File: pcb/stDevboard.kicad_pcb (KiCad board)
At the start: 4 copper layers, 50 x 100 mm, 149 parts, among them IC1 MPM3610GQV-Z, IC2 IRFR9014PBF, IC3 ICM-45686, IC4 ICM-45686, IC5 MMC5983MA, IC6 AT25SF041B-SSHB-B, J1 USB_C_Receptacle_USB2.0_16P, J10 Micro_SD_Card_Det2, J2 USB_C_Receptacle_USB2.0_16P, J4 Conn_02x03_Top_Bottom, J7 73412-0114, J8 73412-0114, Q1 DMN3404L, Q2 MMBT2222A, Q3 DMN3404L, Q4 DMN3404L, Q5 DMN3404L, Q6 DMN3404L, Q7 DMN3404L, Q8 MMBT2222A, U1 BMP581, U2 H3LIS331DLTR, U3 MAX-M10S, U4 STM32U585CIUxQ, U5 STM32U073CCUx, Y1 ECS-TXO-25CSMV-320-AM-TR, Y2 ECS-160-8-36B2-CKM-TR, Y3 CM7V-T1A-32.768KHZ, Y4 CM7V-T1A-32.768KHZ

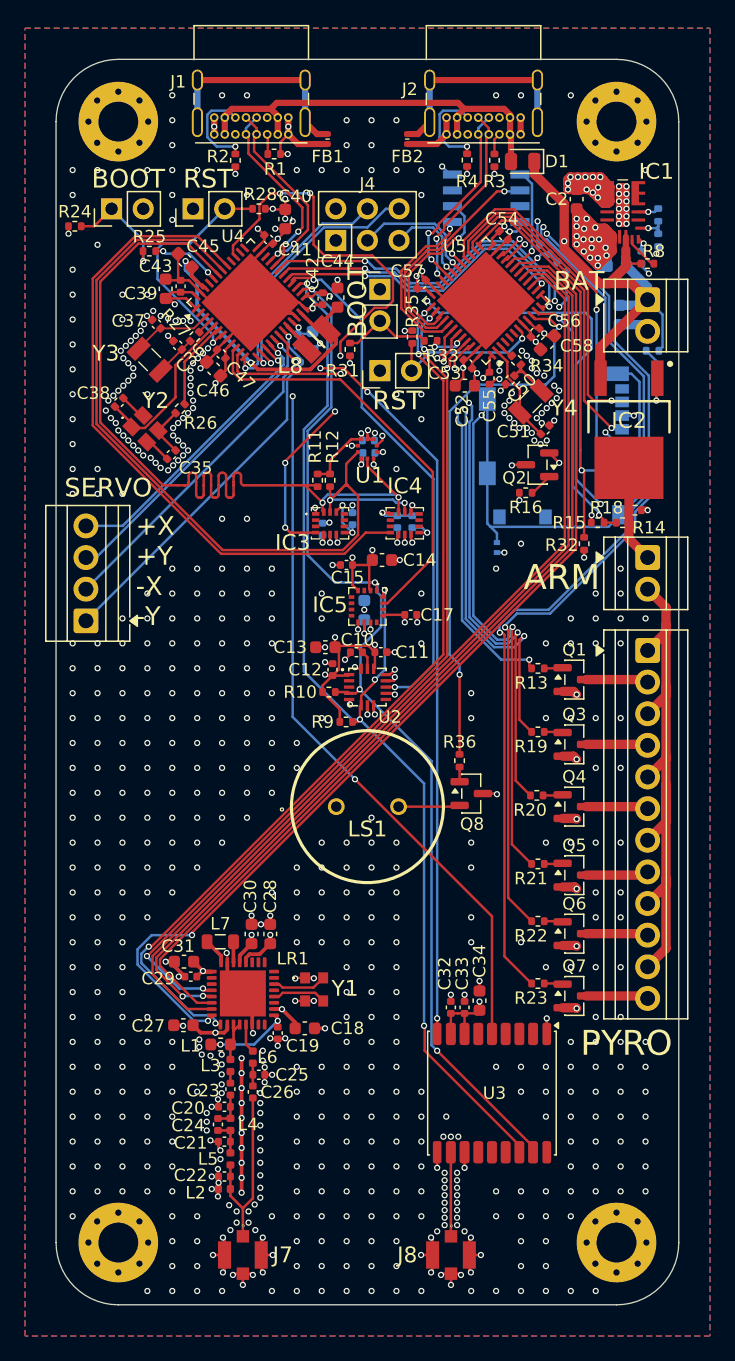
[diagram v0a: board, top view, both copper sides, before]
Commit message: updated pcb from schematic changes, also added some length tuning because why not
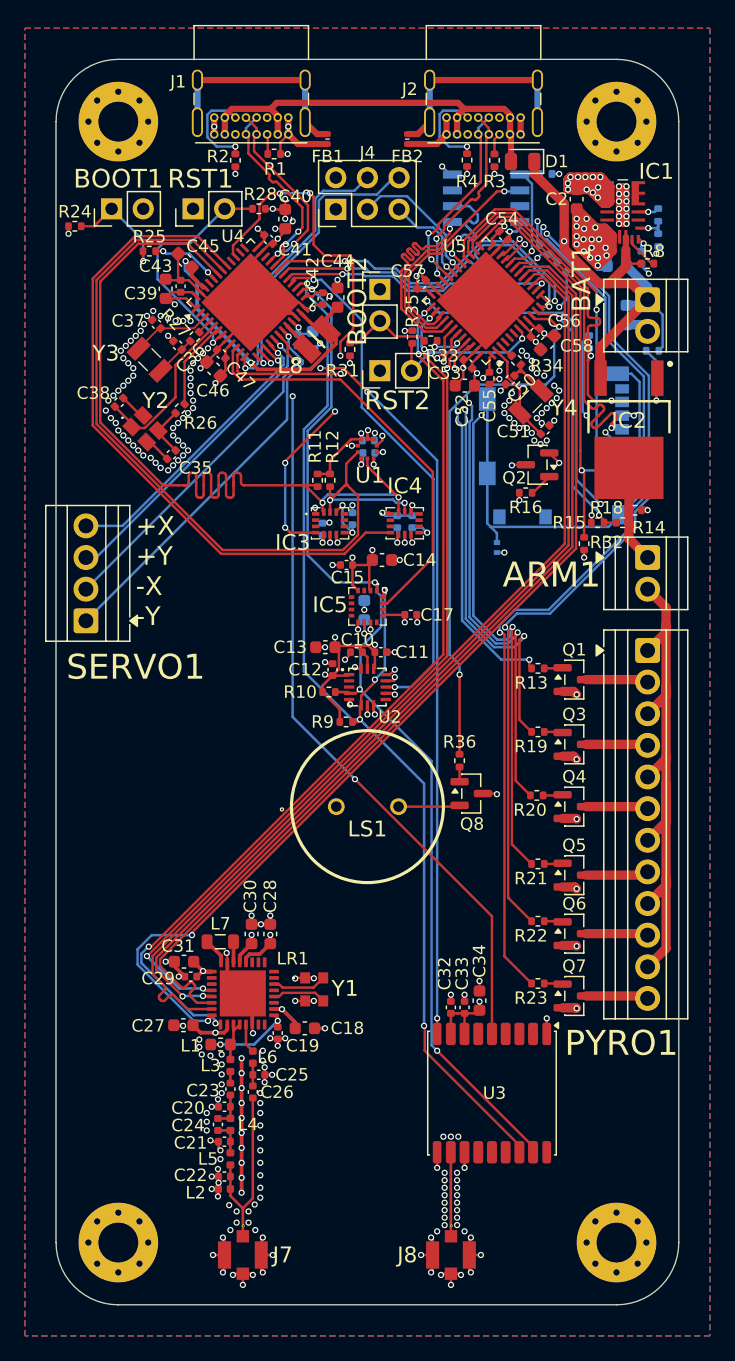
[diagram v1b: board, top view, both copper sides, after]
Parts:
- added R37: 10k, Resistor_SMD:R_0402_1005Metric, B.Cu at (139.3, 84.2)
- added R38: 100k, Resistor_SMD:R_0402_1005Metric, B.Cu at (142.8, 97.7)
- C1: value 100uF -> 22uF
- C39, C46: value 1 uF -> 1uF
- C4, C41, C42, C43, C47, C49, C5: value 100 nF -> 100nF
- C40, C48: value 10 uF -> 10uF
- C44, C45: value 2.2 uF -> 2.2uF
- moved J4 2.50 mm to (122.5, 87.0)
- moved C1 0.55 mm to (145.8, 95.5)
- turned R32 to 90 degrees
- renumbered ARM to ARM1, BAT to BAT1, BOOT to BOOT1, BOOT to BOOT2, PYRO to PYRO1, RST to RST1, RST to RST2, SERVO to SERVO1
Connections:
- R32 pad 1: /peripheral micro/sd_cs -> +3.3V
- R32 pad 2: +3.3V -> /peripheral micro/sd_cs
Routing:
- net +3.3V: track 129.9 -> 137.2 mm, vias 54 -> 56
- net /peripheral micro/sd_clk: track 25.9 -> 30.5 mm
- net usart_ck: track 24.4 -> 28.8 mm
- net /peripheral micro/flash_mosi: track 14.0 -> 18.4 mm
- net imu1_int1: track 48.2 -> 43.9 mm
- net /peripheral micro/flash_clk: track 14.7 -> 18.4 mm
- net /peripheral micro/sd_miso: track 25.7 -> 29.1 mm, vias 1 -> 2
- net mpu_tx_external: track 19.6 -> 22.1 mm
- net mpu_rx_external: track 20.4 -> 23.0 mm
- net arm: track 43.6 -> 41.6 mm
- net spi_sclk: track 77.5 -> 79.0 mm
- net usart_mosi: track 27.4 -> 28.9 mm
- net /peripheral micro/flash_cs: track 9.12 -> 10.5 mm
- net spi_mosi: track 77.9 -> 79.3 mm
- net GND: track 232.0 -> 231.1 mm, vias 713 -> 292
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
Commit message: mainly worked on bom (still just on google sheets), but while doing so fixed some issues and redid some component selection
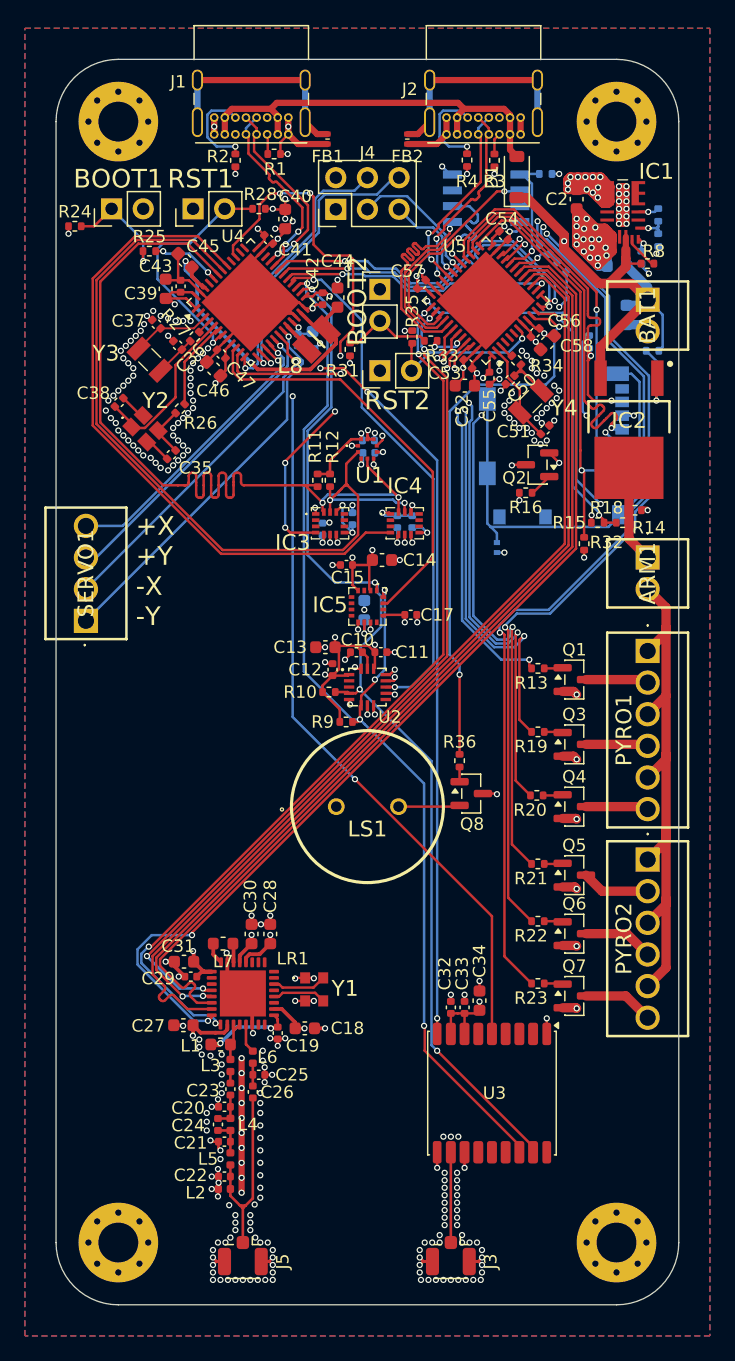
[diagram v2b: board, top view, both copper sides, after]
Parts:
- removed J7, J8: 73412-0114, footprints:73412-0110
- added J3: Conn_Coaxial, Connector_Coaxial:U.FL_Hirose_U.FL-R-SMT-1_Vertical, F.Cu at (131.7, 171.1)
- added J5: Conn_Coaxial, Connector_Coaxial:U.FL_Hirose_U.FL-R-SMT-1_Vertical, F.Cu at (115.0, 171.1)
- added PYRO2: Screw_Terminal_01x06, footprints:TBC05061GG, F.Cu at (147.5, 139.2)
- ARM1, BAT1: footprint TerminalBlock:TerminalBlock_Xinya_XY308-2.54-2P_1x02_P2.54mm_Horizontal -> footprints:TBC05021GG
- D1: footprint Diode_SMD:D_0805_2012Metric -> Diode_SMD:D_SOD-123
- L7: footprint Inductor_SMD:L_0805_2012Metric -> Inductor_SMD:L_0603_1608Metric
- PYRO1: value Screw_Terminal_01x12 -> Screw_Terminal_01x06; footprint TerminalBlock:TerminalBlock_Xinya_XY308-2.54-12P_1x12_P2.54mm_Horizontal -> footprints:TBC05061GG
- SERVO1: footprint TerminalBlock:TerminalBlock_Xinya_XY308-2.54-4P_1x04_P2.54mm_Horizontal -> footprints:TBC05041GG
- moved D1 1.33 mm to (137.0, 84.5), turned to 90 degrees
- moved L7 0.27 mm to (113.4, 146.0)
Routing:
- net GND: track 231.1 -> 219.5 mm, vias 292 -> 320
- net +3.3V: track 137.2 -> 139.7 mm
- net +BATT: track 49.3 -> 48.0 mm
- net +12C: track 46.9 -> 45.8 mm
- net Net-(J5-In): track 15.3 -> 16.3 mm
- net /mosfets/c5_n: track 5.00 -> 5.64 mm
- net /mosfets/c6_n: track 5.03 -> 5.67 mm
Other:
- board text added: "+0 -0 +1 -1 +2 -2 +3 -3 +4 -4 +5 -5"
- board text removed: "+1 -1 +2 -2 +3 -3 +4 -4 +5 -5 +6 -6"

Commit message: reorganized schematic, started to add a readme (not really though), also pcb updated
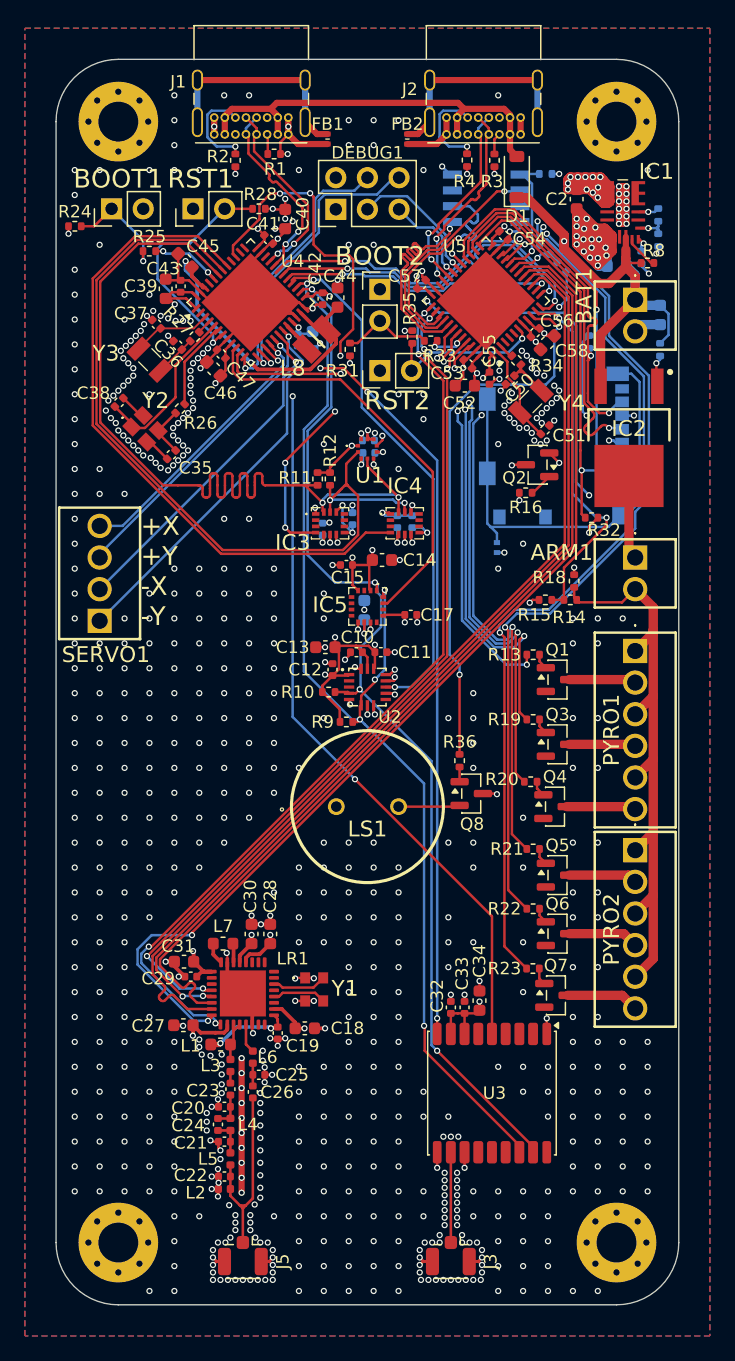
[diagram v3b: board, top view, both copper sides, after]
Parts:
- moved R18 7.50 mm to (141.6, 116.9), turned to -90 degrees
- moved R14 7.49 mm to (141.3, 118.4)
- moved R15 7.49 mm to (139.3, 118.4)
- moved C1 2.70 mm to (148.5, 95.5)
- moved R32 2.17 mm to (143.0, 111.8), turned to 180 degrees
- moved Q4 1.55 mm to (140.1, 135.0)
- moved Q7 1.48 mm to (140.1, 150.2)
- moved Q1 1.35 mm to (140.3, 124.8)
- moved Q3 1.35 mm to (140.3, 130.0)
- moved Q5 1.35 mm to (140.3, 140.5)
- moved Q6 1.35 mm to (140.3, 145.2)
- moved R23 1.26 mm to (138.3, 148.0)
- moved R21 1.26 mm to (138.3, 138.4)
- moved PYRO2 1.25 mm to (146.5, 138.5)
- moved R20 1.20 mm to (138.1, 133.0)
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- renumbered J4 to DEBUG1
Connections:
- net /shutupdrc renamed /x
- net Net-(IC5-CAP) renamed /sensors/mag_cap
- net Net-(J5-In) renamed /rf/lr_pre_rfin
- net Net-(LR1-RFI_LF) renamed /rf/lr_rfin
- net Net-(LR1-RFO_LF1) renamed /rf/lr_rfout
- net Net-(LR1-VTCXO/VNTC) renamed /rf/txco_vdd
- net Net-(LR1-XTA) renamed /rf/txco_out
- net Net-(RST1-Pin_2) renamed /main micro/reset
- net Net-(RST2-Pin_2) renamed /peripheral micro/reset
- net Net-(U4-PC14) renamed /main micro/lse_A
- net Net-(U4-PC15) renamed /main micro/lse_B
- net Net-(U4-PH0) renamed /main micro/hse_A
- net Net-(U4-PH1) renamed /main micro/hse_B
- net Net-(U4-PH3) renamed /main micro/boot
- net Net-(U5-PA0) renamed /peripheral micro/piezo
- net Net-(U5-PC13) renamed /peripheral micro/lse_A
- net Net-(U5-PC14) renamed /peripheral micro/lse_B
- net Net-(U5-PF3) renamed /peripheral micro/boot
- net imu3_int1 renamed accel_int1
- ARM1 pad 2: +12C -> +BATT_SWITCHED
- C10 pad 1: +3.3V -> GND
- C10 pad 2: GND -> +3.3V
- C11 pad 1: +3.3V -> GND
- C11 pad 2: GND -> +3.3V
- C12 pad 1: +3.3V -> GND
- C12 pad 2: GND -> +3.3V
- C13 pad 1: +3.3V -> GND
- C13 pad 2: GND -> +3.3V
- C28 pad 1: +3.3V -> GND
- C28 pad 2: GND -> +3.3V
- C30 pad 1: +3.3V -> GND
- C30 pad 2: GND -> +3.3V
- C32 pad 1: +3.3V -> GND
- C32 pad 2: GND -> +3.3V
- C35 pad 2: Net-(Y2-GND_1) -> GND
- C36 pad 1: GND -> Net-(C36-Pad1)
- C36 pad 2: Net-(C36-Pad2) -> GND
- C38 pad 2: Net-(Y2-GND_2) -> GND
- C39 pad 1: GND -> +3.3V
- C39 pad 2: +3.3V -> GND
- C40 pad 1: GND -> +3.3V
- C40 pad 2: +3.3V -> GND
- C41 pad 1: GND -> +3.3V
- C41 pad 2: +3.3V -> GND
- C42 pad 1: GND -> +3.3V
- C42 pad 2: +3.3V -> GND
- C43 pad 1: GND -> +3.3V
- C43 pad 2: +3.3V -> GND
- C44 pad 1: Net-(C44-Pad1) -> /main micro/vdd11
- C45 pad 1: Net-(C44-Pad1) -> /main micro/vdd11
- C46 pad 1: GND -> +3.3V
- C46 pad 2: +3.3V -> GND
- C47 pad 1: GND -> +3.3V
- C47 pad 2: +3.3V -> GND
- C50 pad 1: GND -> Net-(C50-Pad1)
- C50 pad 2: Net-(C50-Pad2) -> GND
- C52 pad 1: GND -> +3.3V
- C52 pad 2: +3.3V -> GND
- C53 pad 1: GND -> +3.3V
- C53 pad 2: +3.3V -> GND
- C54 pad 1: +3.3V -> GND
- C54 pad 2: GND -> +3.3V
- C55 pad 1: +3.3V -> GND
- C55 pad 2: GND -> +3.3V
- C56 pad 1: +3.3V -> GND
- C56 pad 2: GND -> +3.3V
- C57 pad 1: GND -> +3.3V
- C57 pad 2: +3.3V -> GND
- C58 pad 1: GND -> +3.3V
- C58 pad 2: +3.3V -> GND
- L8 pad 1: Net-(U4-VLXSMPS) -> /main micro/vdd11
- L8 pad 2: Net-(C44-Pad1) -> Net-(U4-VLXSMPS)
- PYRO1 pad 1: +12C -> +BATT_SWITCHED
- PYRO1 pad 2: /mosfets/c1_n -> /mosfets/c0_n
- PYRO1 pad 3: +12C -> +BATT_SWITCHED
- PYRO1 pad 4: /mosfets/c2_n -> /mosfets/c1_n
- PYRO1 pad 5: +12C -> +BATT_SWITCHED
- PYRO1 pad 6: /mosfets/c3_n -> /mosfets/c2_n
- PYRO2 pad 1: +12C -> +BATT_SWITCHED
- PYRO2 pad 2: /mosfets/c4_n -> /mosfets/c3_n
- PYRO2 pad 3: +12C -> +BATT_SWITCHED
- PYRO2 pad 4: /mosfets/c5_n -> /mosfets/c4_n
- PYRO2 pad 5: +12C -> +BATT_SWITCHED
- PYRO2 pad 6: /mosfets/c6_n -> /mosfets/c5_n
- Q1 pad 3: /mosfets/c1_n -> /mosfets/c0_n
- Q3 pad 3: /mosfets/c2_n -> /mosfets/c1_n
- Q4 pad 3: /mosfets/c3_n -> /mosfets/c2_n
- Q5 pad 3: /mosfets/c4_n -> /mosfets/c3_n
- Q6 pad 3: /mosfets/c5_n -> /mosfets/c4_n
- Q7 pad 3: /mosfets/c6_n -> /mosfets/c5_n
- R14 pad 2: Net-(ARM1-Pin_1) -> +BATT_SWITCHED
- R18 pad 1: Net-(ARM1-Pin_1) -> +3.3V
- R18 pad 2: +3.3V -> +BATT_SWITCHED
- R27 pad 1: Net-(C36-Pad2) -> Net-(C36-Pad1)
- R34 pad 1: Net-(C50-Pad2) -> Net-(C50-Pad1)
- U4 pad 23: Net-(C44-Pad1) -> /main micro/vdd11
- U4 pad 46: Net-(C44-Pad1) -> /main micro/vdd11
- U5 pad 12: usart_mosi -> usart_miso
- U5 pad 13: usart_miso -> usart_mosi
- Y2 pad 2: Net-(Y2-GND_1) -> GND
- Y2 pad 4: Net-(Y2-GND_2) -> GND
- Y3 pad 2: Net-(C36-Pad2) -> Net-(C36-Pad1)
- Y4 pad 2: Net-(C50-Pad2) -> Net-(C50-Pad1)
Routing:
- net +BATT_SWITCHED: track 0.00 -> 49.1 mm
- net +12C: track 45.8 -> 0.00 mm
- net Net-(C44-Pad1): track 27.3 -> 0.00 mm, vias 2 -> 0
- net /main micro/vdd11: track 0.00 -> 27.3 mm, vias 0 -> 2
- net cont_test_out: track 21.0 -> 29.1 mm
- net /mosfets/c6_n: track 5.67 -> 0.00 mm
- net /mosfets/c0_n: track 0.00 -> 5.40 mm
- net Net-(C50-Pad2): track 4.27 -> 0.00 mm
- net Net-(C50-Pad1): track 0.00 -> 4.27 mm
- net Net-(C36-Pad2): track 3.36 -> 0.00 mm
- net Net-(C36-Pad1): track 0.00 -> 3.36 mm
- net +BATT: track 48.0 -> 45.6 mm
- net Net-(Y2-GND_1): track 2.20 -> 0.00 mm
- net Net-(Y2-GND_2): track 2.18 -> 0.00 mm
- net GND: track 219.5 -> 217.3 mm, vias 320 -> 718
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
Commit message: added camera high side switching
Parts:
- added CAM1: Screw_Terminal_01x02, footprints:TBC05021GG, F.Cu at (103.5, 137.5)
- added IC7: IRFR9014PBF, footprints:TO228P990X238-3N, F.Cu at (111.5, 131.9)
- added Q9: MMBT2222A, Package_TO_SOT_SMD:SOT-23, F.Cu at (115.1, 124.0)
- added R39: 1k, Resistor_SMD:R_0402_1005Metric, F.Cu at (114.2, 121.1)
- added R40: 10k, Resistor_SMD:R_0402_1005Metric, F.Cu at (111.5, 125.5)
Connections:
- U5 pad 34: unconnected-(U5-PA13-Pad34) -> cam_enable
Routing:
- net +BATT: track 45.6 -> 114.4 mm, vias 2 -> 5
- net cam_enable: track 0.00 -> 39.7 mm, vias 0 -> 5
- net Net-(CAM1-Pin_2): track 0.00 -> 8.00 mm
- net GND: track 217.3 -> 224.9 mm, vias 718 -> 682
- net Net-(IC7-G): track 0.00 -> 6.03 mm
- net +3.3V: track 138.7 -> 142.9 mm, vias 56 -> 55
- net Net-(IC2-G): track 18.0 -> 15.2 mm
- net Net-(Q9-B): track 0.00 -> 1.46 mm
- net arm: track 39.8 -> 39.1 mm
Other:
- board text added: "+ -"

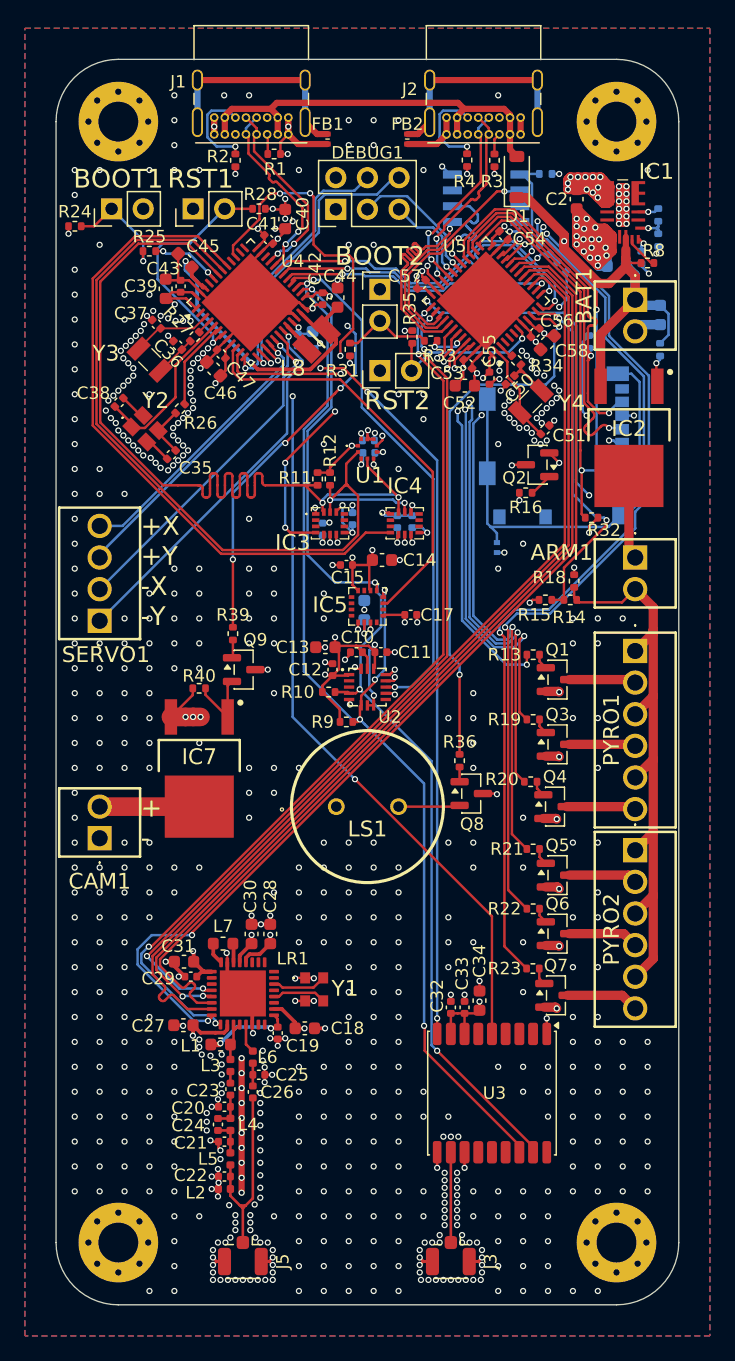
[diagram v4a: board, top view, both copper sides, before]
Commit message: modified gps for an active antenna
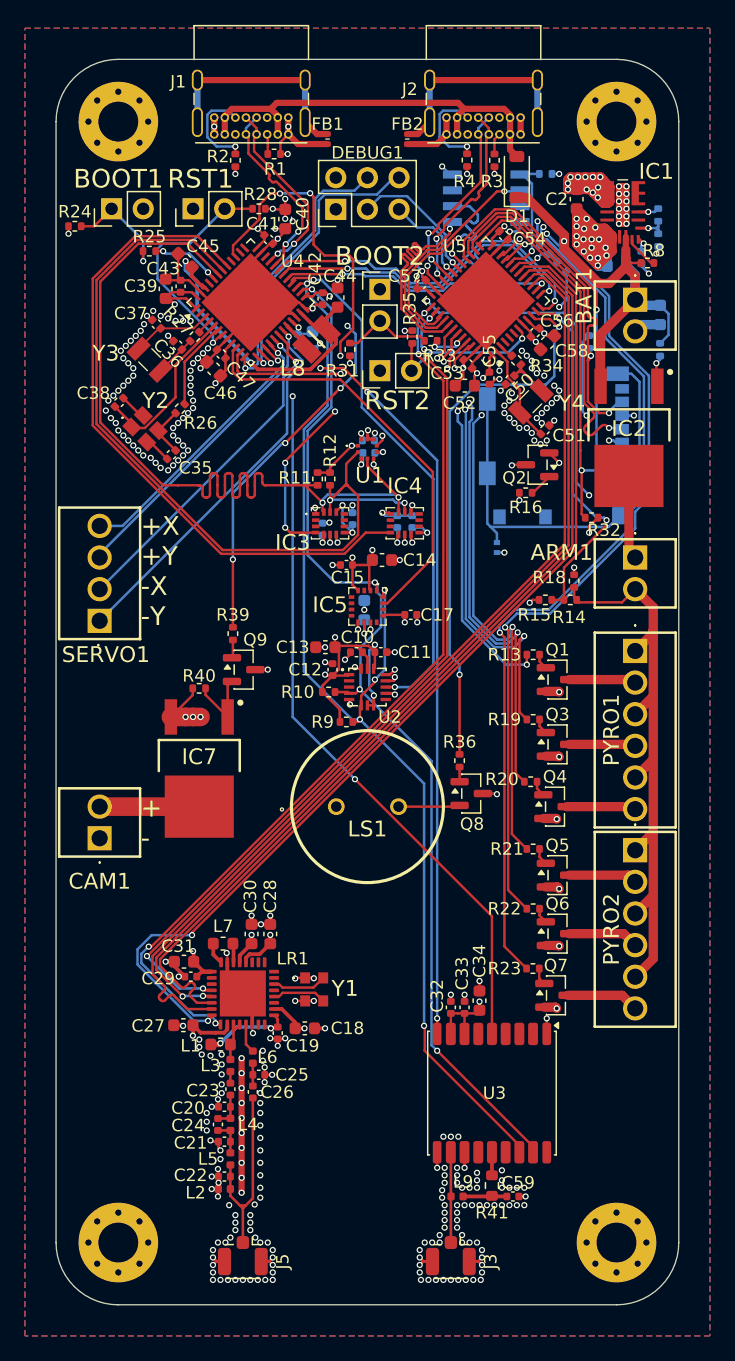
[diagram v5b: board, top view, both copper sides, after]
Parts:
- added C59: 10nF, Capacitor_SMD:C_0402_1005Metric, F.Cu at (136.7, 166.3)
- added L9: 27nH, Inductor_SMD:L_0402_1005Metric, F.Cu at (132.2, 166.3)
- added R41: 10, Resistor_SMD:R_0603_1608Metric, F.Cu at (135.0, 165.4)
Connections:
- U3 pad 14: unconnected-(U3-VCC_RF-Pad14) -> Net-(U3-VCC_RF)
- U4 pad 40: Net-(D2-A) -> unconnected-(U4-PB4-Pad40)
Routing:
- net Net-(C59-Pad1): track 0.00 -> 3.56 mm
- net Net-(U3-VCC_RF): track 0.00 -> 1.85 mm
- net GND: track 224.9 -> 226.2 mm, vias 682 -> 342
